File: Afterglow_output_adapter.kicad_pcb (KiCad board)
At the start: 2 copper layers, 25.4 x 96.5 mm, 3 parts, among them J1 Afterglow, J2 Playfield_Col, J3 Playfield_Col

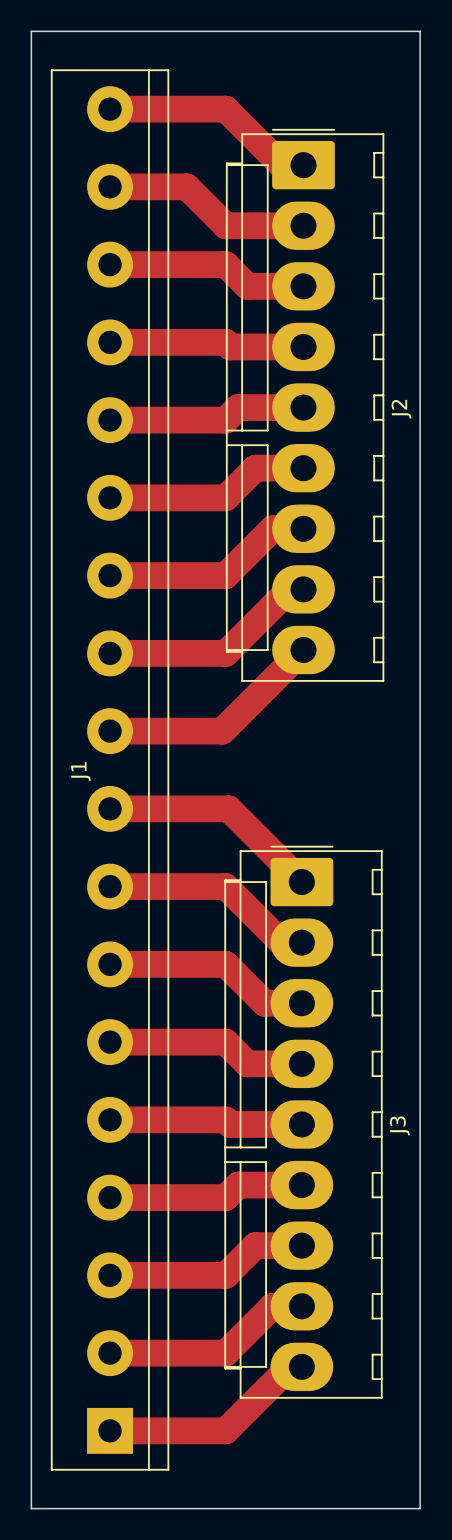
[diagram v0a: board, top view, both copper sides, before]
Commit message: Removed unwanted files and changed licence to CC NC
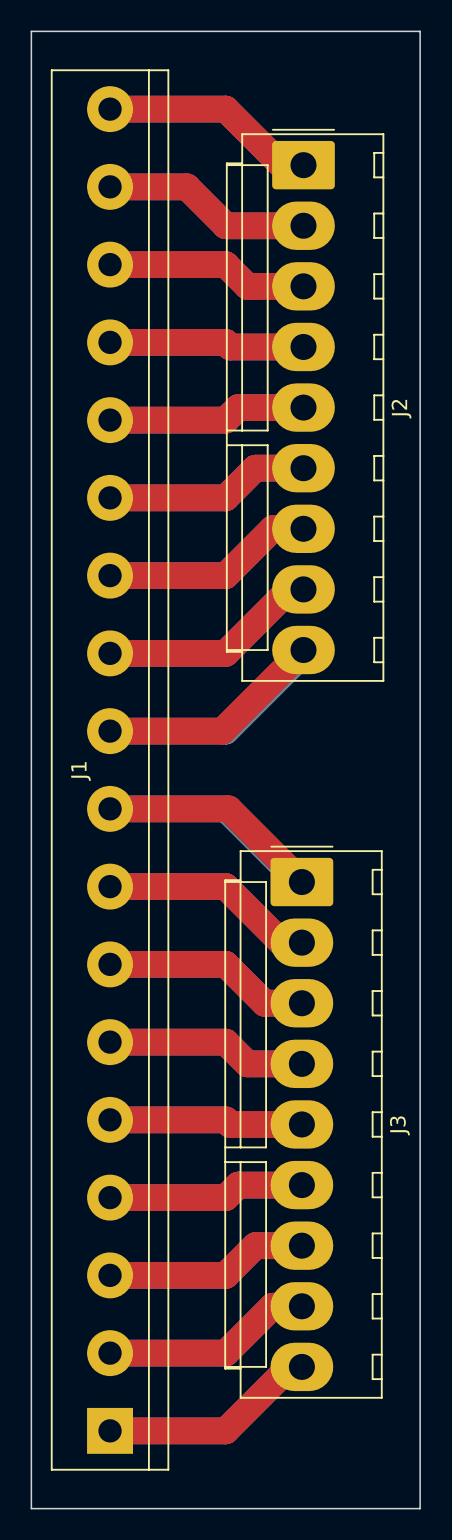
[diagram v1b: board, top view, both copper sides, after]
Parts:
- J2: value Playfield_Col -> Columns
- J3: value Playfield_Col -> Rows
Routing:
- net Net-(J1-Pin_10): track 14.9 -> 29.9 mm
- net Net-(J1-Pin_9): track 14.6 -> 29.1 mm
- net Net-(J1-Pin_11): track 14.4 -> 28.8 mm
- net Net-(J1-Pin_1): track 14.3 -> 28.6 mm
- net Net-(J1-Pin_18): track 14.2 -> 28.4 mm
- net Net-(J1-Pin_8): track 14.1 -> 28.2 mm
- net Net-(J1-Pin_12): track 14.0 -> 27.9 mm
- net Net-(J1-Pin_2): track 13.9 -> 27.7 mm
- net Net-(J1-Pin_17): track 13.8 -> 27.4 mm
- net Net-(J1-Pin_7): track 13.6 -> 27.2 mm
- net Net-(J1-Pin_13): track 13.5 -> 26.9 mm
- net Net-(J1-Pin_3): track 13.4 -> 26.7 mm
- net Net-(J1-Pin_6): track 13.2 -> 26.3 mm
- net Net-(J1-Pin_14): track 13.0 -> 26.0 mm
- net Net-(J1-Pin_4): track 12.9 -> 25.8 mm
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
